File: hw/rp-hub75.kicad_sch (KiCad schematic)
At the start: 38 parts, among them J1 Display Connector, J2 USB_C_Receptacle_USB2.0_16P, J3 Screw_Terminal_01x02, J4 Conn_01x04, J5 USB_A, J6 Conn_01x10, U1 AMS1117-3.3, U2 RP2350_60QFN, U3 W25Q128JVS, Y1 TXM12M0004322CBCDO00T

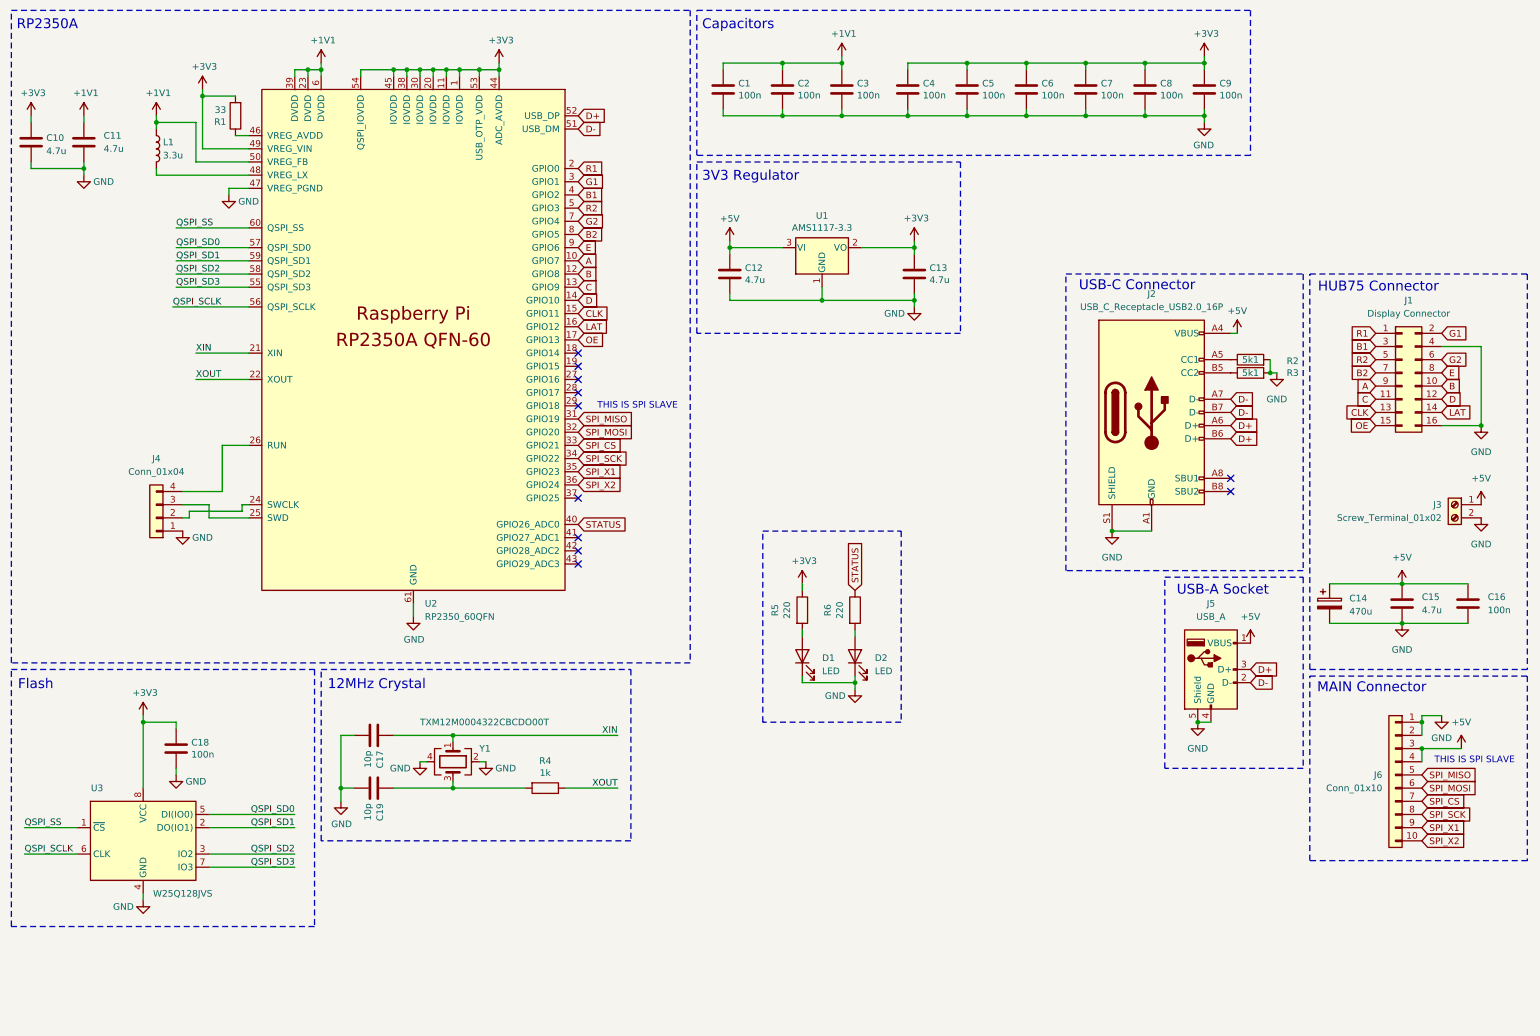
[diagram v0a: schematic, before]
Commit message: hw: edit DBG connector, new capacitor
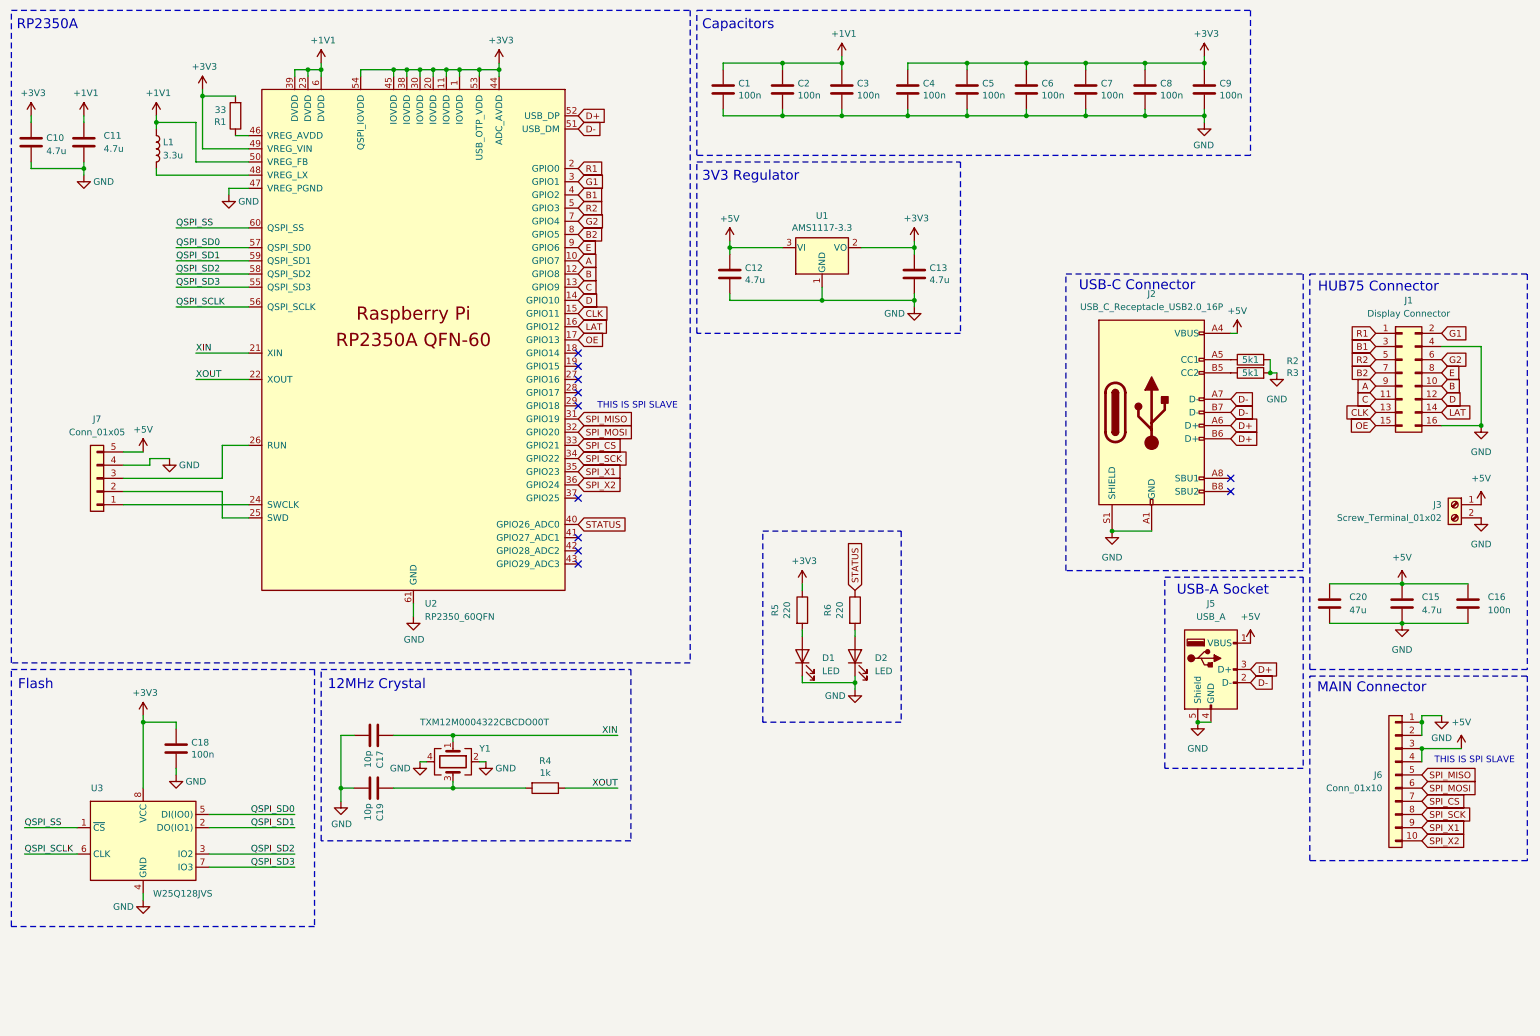
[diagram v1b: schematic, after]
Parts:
- removed C14: 470u, Capacitor_SMD:CP_Elec_6.3x7.7, symbol Device:C_Polarized
- removed J4: Conn_01x04, Connector_PinHeader_2.54mm:PinHeader_1x04_P2.54mm_Vertical, symbol Connector_Generic:Conn_01x04
- added C20: 47u, Capacitor_SMD:C_1206_3216Metric, symbol Device:C
- added J7: Conn_01x05, Connector_PinHeader_2.54mm:PinHeader_1x05_P2.54mm_Vertical, symbol Connector_Generic:Conn_01x05
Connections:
- net +5V: now also C20.1, J7.5 (Pin_5)
- net GND: now also C20.2, J7.4 (Pin_4)
- net at U2.24 (SWCLK): now also J7.1 (Pin_1)
- net at U2.25 (SWD): now also J7.2 (Pin_2)
- net at U2.26 (RUN): now also J7.3 (Pin_3)

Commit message: V1.2
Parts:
- added J4: Conn_01x02, Connector_PinHeader_2.54mm:PinHeader_1x02_P2.54mm_Vertical, symbol Connector_Generic:Conn_01x02
- J7: now not fitted; now left out of the parts list
- R5, R6: value 220 -> 1k; LCSC C25091 -> C11702
- U3: value W25Q128JVS -> ZD25WQ80CTIGT; footprint Package_SO:SOIC-8_5.3x5.3mm_P1.27mm -> Package_SO:SOIC-8_3.9x4.9mm_P1.27mm; LCSC C113767 -> C7525143
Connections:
- net +5V: now also J3.2 (Pin_2), J7.2 (Pin_2); no longer J3.1 (Pin_1), J7.5 (Pin_5)
- net GND: now also J3.1 (Pin_1), J7.1 (Pin_1), J4.1 (Pin_1); no longer J3.2 (Pin_2), J7.4 (Pin_4)
- net QSPI_SS: now also J4.2 (Pin_2)
- net at U2.24 (SWCLK): now also J7.3 (Pin_3); no longer J7.1 (Pin_1)
- net at U2.25 (SWD): now also J7.4 (Pin_4); no longer J7.2 (Pin_2)
- net at U2.26 (RUN): now also J7.5 (Pin_5); no longer J7.3 (Pin_3)
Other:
- moved on the sheet: J3

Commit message: V1.3
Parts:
- added J8: Conn_01x04, Connector_PinHeader_2.54mm:PinHeader_1x04_P2.54mm_Vertical, symbol Connector_Generic:Conn_01x04
- renumbered C18 to C10, C10 to C11, C6 to C17, C17 to C18, C11 to C4, C4 to C5, C5 to C6
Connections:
- net +5V: now also J6.2 (Pin_2), J8.1 (Pin_1); no longer J6.4 (Pin_4)
- net D+: now also J8.3 (Pin_3)
- net D-: now also J8.2 (Pin_2)
- net GND: now also J6.8 (Pin_8), J8.4 (Pin_4); no longer J6.2 (Pin_2)
- net SPI_CS: now also J6.6 (Pin_6); no longer J6.7 (Pin_7)
- net SPI_MISO: now also J6.4 (Pin_4); no longer J6.5 (Pin_5)
- net SPI_MOSI: now also J6.5 (Pin_5); no longer J6.6 (Pin_6)
- net SPI_SCK: now also J6.7 (Pin_7); no longer J6.8 (Pin_8)
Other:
- note added: "PWR & DBG leds"
- note added: "RP2350 Capacitors"
- note added: "THIS BOARD IS SPI SLAVE"
- note removed: "Capacitors"
- note removed: "THIS IS SPI SLAVE"
- moved on the sheet: C10, C11, C12, C13, C15, C16, C17, C20, C4, C5, C6, D1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

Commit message: V1.4
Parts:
- removed J4: Conn_01x02, Connector_PinHeader_2.54mm:PinHeader_1x02_P2.54mm_Vertical, symbol Connector_Generic:Conn_01x02
- added SW1: SW_Push, Button_Switch_SMD:SW_SPST_TS-1088-xR025, symbol Switch:SW_Push
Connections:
- net GND: now also SW1.1
- net QSPI_SS: now also SW1.2
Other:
- moved on the sheet: C17, U3

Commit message: V1.4b
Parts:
- removed C20: 47u, Capacitor_SMD:C_1206_3216Metric, symbol Device:C
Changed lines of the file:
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@@
 	)
 	(junction
-		(at 279.4 217.17)
-		(diameter 0)
-		(color 0 0 0 0)
-	)
-	(junction
 		(at 170.18 85.09)
 		(diameter 0)
@@
 	)
 	(junction
-		(at 279.4 209.55)
-		(diameter 0)
-		(color 0 0 0 0)
-	)
-	(junction
 		(at 158.75 85.09)
 		(diameter 0)
@@
 	(wire
 		(pts
-			(xy 265.43 217.17) (xy 279.4 217.17)
-		)
-		(stroke
-			(width 0)
-			(type default)
-		)
-	)
-	(wire
-		(pts
 			(xy 163.83 261.62) (xy 146.05 261.62)
 		)
@@
 	(wire
 		(pts
-			(xy 265.43 209.55) (xy 279.4 209.55)
-		)
-		(stroke
-			(width 0)
-			(type default)
-		)
-	)
-	(wire
-		(pts
 			(xy 264.16 92.71) (xy 264.16 93.98)
 		)
@@
 					(unit 1)
 				)
-			)
-		)
-	)
-	(symbol
-		(lib_id "Device:C")
-		(at 265.43 213.36 0)
-		(unit 1)
-		(exclude_from_sim no)
-		(in_bom yes)
-		(on_board yes)
-		(dnp no)
-		(fields_autoplaced yes)
-		(property "Reference" "C20"
-			(at 269.24 212.0899 0)
-			(effects
-				(font
-					(size 1.27 1.27)
-				)
-				(justify left)
-			)
-		)
-		(property "Value" "47u"
-			(at 269.24 214.6299 0)
-			(effects
-				(font
-					(size 1.27 1.27)
-				)
-				(justify left)
-			)
-		)
-		(property "Footprint" "Capacitor_SMD:C_1206_3216Metric"
-			(at 266.3952 217.17 0)
-			(effects
-				(font
-					(size 1.27 1.27)
-				)
-				(hide yes)
-			)
-		)
-		(property "Datasheet" "~"
-			(at 265.43 213.36 0)
-			(effects
-				(font
-					(size 1.27 1.27)
-				)
-				(hide yes)
-			)
-		)
-		(property "Description" "Unpolarized capacitor"
-			(at 265.43 213.36 0)
-			(effects
-				(font
-					(size 1.27 1.27)
-				)
-				(hide yes)
-			)
-		)
-		(property "LCSC" "C96123"
-			(at 265.43 213.36 0)
-			(effects
-				(font
-					(size 1.27 1.27)
-				)
-				(hide yes)
-			)
-		)
-		(pin "1"
-		)
-		(pin "2"
-		)
-		(instances
-			(project "rp-hub75"
-				(path "/b3849755-2bc4-4a7c-8e78-ae8190aa99e0"
-					(reference "C20")
-					(unit 1)
-				)
